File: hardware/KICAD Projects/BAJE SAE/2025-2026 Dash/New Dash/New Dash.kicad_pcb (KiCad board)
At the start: 2 copper layers, 1 part, among them U1 XIAO-ESP32-S3-SMD

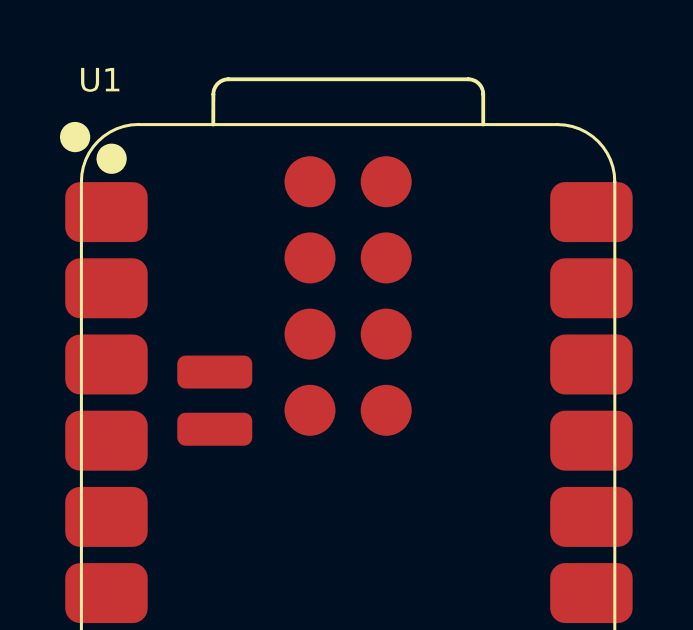
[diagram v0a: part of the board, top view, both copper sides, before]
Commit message: Pasted in the rest of the components
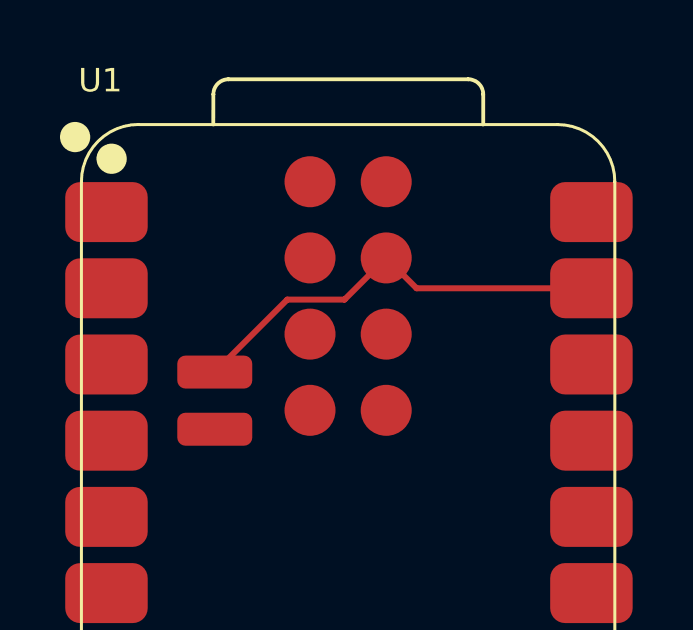
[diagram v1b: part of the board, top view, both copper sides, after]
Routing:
- net GND: track 0.00 -> 14.6 mm
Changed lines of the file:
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@@
 		(embedded_fonts no)
+	)
+	(segment
+		(start 42.271 37.677)
+		(end 40.361 37.677)
+		(width 0.2)
+		(layer "F.Cu")
+		(net 11)
+	)
+	(segment
+		(start 40.361 37.677)
+		(end 37.945 40.093)
+		(width 0.2)
+		(layer "F.Cu")
+		(net 11)
+	)
+	(segment
+		(start 44.672 37.3)
+		(end 43.66 36.288)
+		(width 0.2)
+		(layer "F.Cu")
+		(net 11)
+	)
+	(segment
+		(start 43.66 36.288)
+		(end 42.271 37.677)
+		(width 0.2)
+		(layer "F.Cu")
+		(net 11)
+	)
+	(segment
+		(start 50.5 37.3)
+		(end 44.672 37.3)
+		(width 0.2)
+		(layer "F.Cu")
+		(net 11)
 	)
 	(embedded_fonts no)

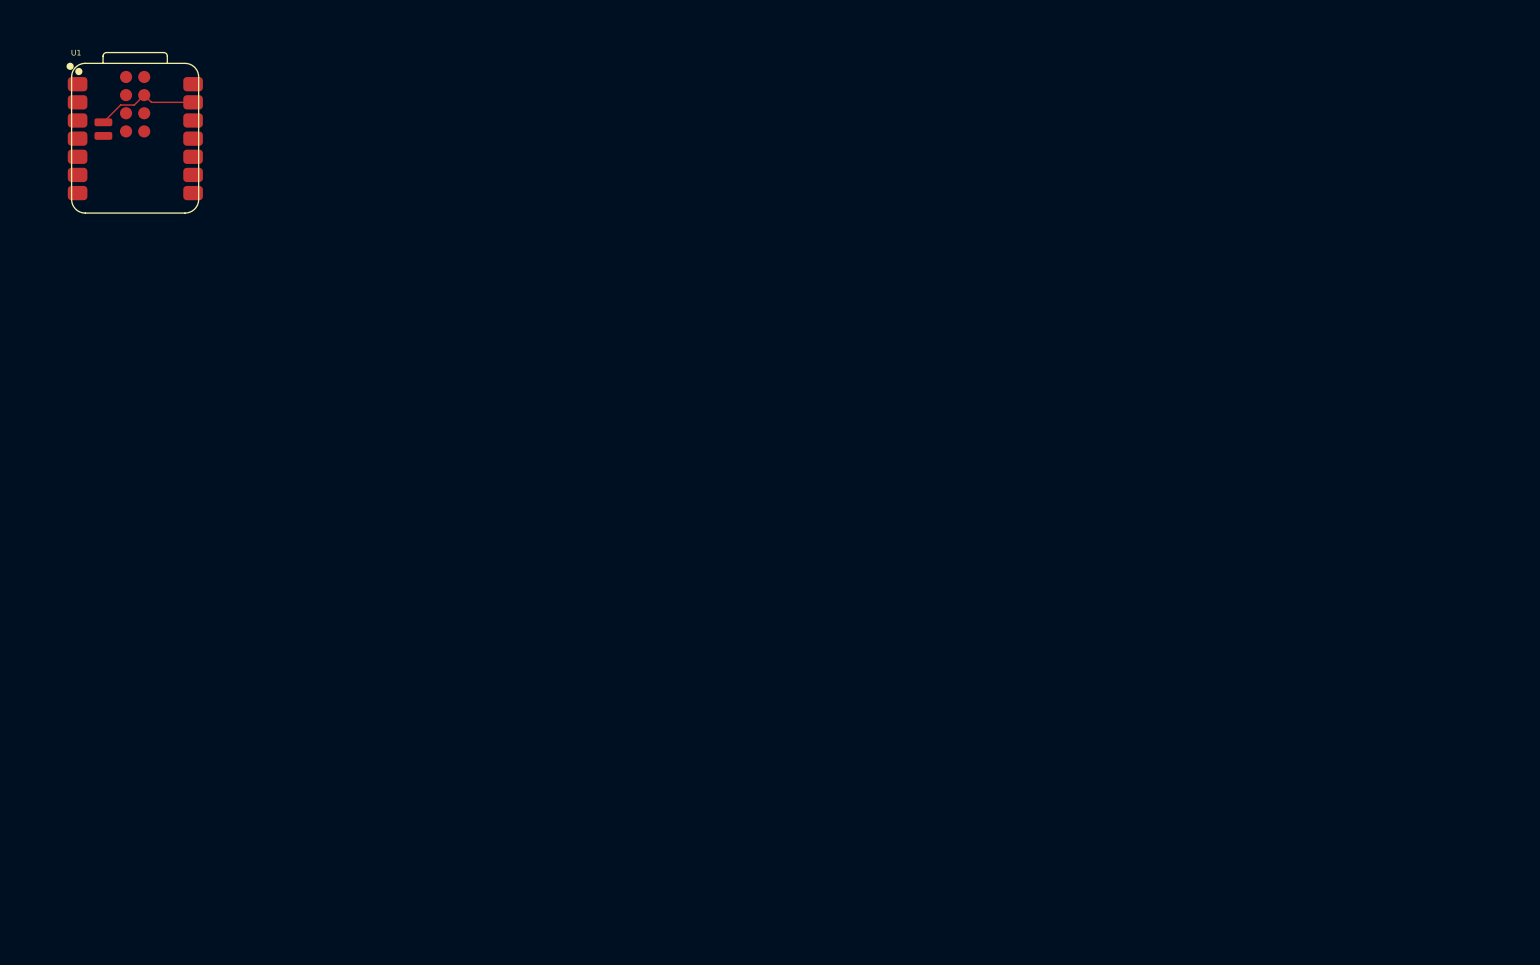
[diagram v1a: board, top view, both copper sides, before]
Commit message: Updating Final Dash setup
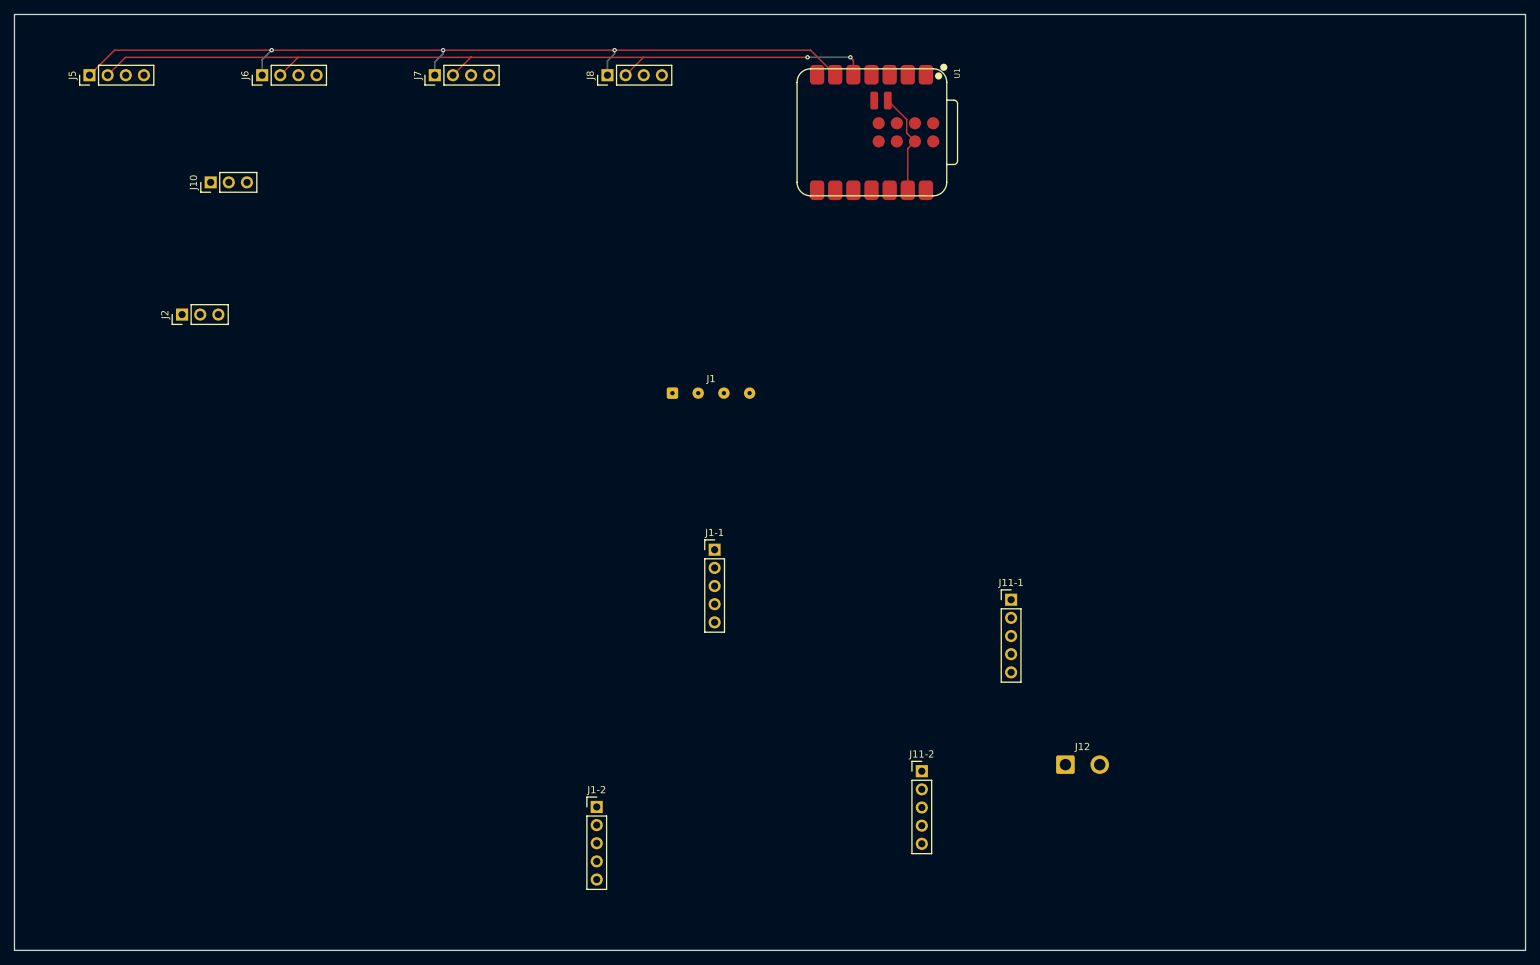
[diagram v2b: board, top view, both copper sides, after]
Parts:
- added J1: CAN to outer connector, Connector_Wire:SolderWire-0.1sqmm_1x04_P3.6mm_D0.4mm_OD1mm, F.Cu at (117.6, 78.0)
- added J1-1: Conn_01x05, Connector_PinHeader_2.54mm:PinHeader_1x05_P2.54mm_Vertical, F.Cu at (123.5, 99.9)
- added J1-2: Conn_01x05, Connector_PinHeader_2.54mm:PinHeader_1x05_P2.54mm_Vertical, F.Cu at (107.0, 135.9)
- added J10: Servo 1 (RPM), Connector_PinHeader_2.54mm:PinHeader_1x03_P2.54mm_Vertical, F.Cu at (53.0, 48.5)
- added J11-1: Conn_01x05, Connector_PinHeader_2.54mm:PinHeader_1x05_P2.54mm_Vertical, F.Cu at (165.0, 106.9)
- added J11-2: Conn_01x05, Connector_PinHeader_2.54mm:PinHeader_1x05_P2.54mm_Vertical, F.Cu at (152.5, 130.9)
- added J12: Conn_01x02, Connector_Wire:SolderWire-0.75sqmm_1x02_P4.8mm_D1.25mm_OD2.3mm, F.Cu at (172.6, 130.0)
- added J2: Servo 2 (Speed), Connector_PinHeader_2.54mm:PinHeader_1x03_P2.54mm_Vertical, F.Cu at (49.0, 67.0)
- added J5: Alpha 1, Connector_PinHeader_2.54mm:PinHeader_1x04_P2.54mm_Vertical, F.Cu at (36.0, 33.5)
- added J6: Alpha 2, Connector_PinHeader_2.54mm:PinHeader_1x04_P2.54mm_Vertical, F.Cu at (60.2, 33.5)
- added J7: Alpha 3, Connector_PinHeader_2.54mm:PinHeader_1x04_P2.54mm_Vertical, F.Cu at (84.3, 33.5)
- added J8: Alpha 4, Connector_PinHeader_2.54mm:PinHeader_1x04_P2.54mm_Vertical, F.Cu at (108.5, 33.5)
- moved U1 103.1 mm to (145.5, 41.5), turned to -90 degrees
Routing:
- net SCL: track 0.00 -> 119.2 mm, vias 0 -> 3
- net SDA: track 0.00 -> 118.3 mm, vias 0 -> 2
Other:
- board outline added: 211.5 x 131 mm
